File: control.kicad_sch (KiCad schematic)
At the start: 0 parts

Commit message: split into multiple sheets
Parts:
- added C1, C2: 10µF, Capacitor_SMD:C_0402_1005Metric, symbol Device:C_Small
- added C10, C8, C9: 4.7µF, Capacitor_SMD:C_0402_1005Metric, symbol Device:C_Small
- added C11: 10nF, Capacitor_SMD:C_0402_1005Metric, symbol Device:C_Small
- added C12: 1µF, Capacitor_SMD:C_0402_1005Metric, symbol Device:C_Small
- added C3, C4, C5, C6, C7: 100nF, Capacitor_SMD:C_0402_1005Metric, symbol Device:C_Small
- added F1: Fuse, symbol Device:Fuse
- added FB1: 100Ohm @ 100MHz, symbol Device:Ferrite_Bead_Small
- added J1: USB_OTG, symbol Connector:USB_OTG
- added J2: Conn_01x04_Male, symbol Connector:Conn_01x04_Male
- added J5: Conn_ARM_JTAG_SWD_10, symbol Connector:Conn_ARM_JTAG_SWD_10
- added JP1: SolderJumper_3_Bridged12, symbol Jumper:SolderJumper_3_Bridged12
- added JP2: SolderJumper_2_Open, symbol Jumper:SolderJumper_2_Open
- added R5: 10kΩ, symbol Device:R_Small
- added U2: AMS1117-3.3, Package_TO_SOT_SMD:SOT-223-3_TabPin2, symbol Regulator_Linear:AMS1117-3.3
- added U3: STM32F042C4Tx, Package_QFP:LQFP-48_7x7mm_P0.5mm, symbol MCU_ST_STM32F0:STM32F042C4Tx
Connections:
- new net: F1.2, FB1.1
- new net: C1.1, FB1.2, U2.3 (VI)
- new net: J2.1 (Pin_1), JP1.2 (C)
- new net +3V3: C10.1, C11.1, C12.1, C2.1, C3.1, C4.1, C5.1, C6.1, C7.1, C8.1, C9.1, J5.1 (VTref), JP1.1 (A), JP2.2 (B), U2.2 (VO), U3.1 (VBAT), U3.24 (VDD), U3.36 (VDDIO2), U3.48 (VDD), U3.9 (VDDA)
- new net +5V: F1.1, J1.1 (VBUS), JP1.3 (B)
- new net BOOT0: JP2.1 (A), R5.1, U3.44 (PF11)
- new net GND: C1.2, C10.2, C11.2, C12.2, C2.2, C3.2, C4.2, C5.2, C6.2, C7.2, C8.2, C9.2, J1.4 (ID), J1.5 (GND), J2.4 (Pin_4), J5.3 (GND), J5.5 (GND), J5.9 (GNDDetect), R5.2, U2.1 (GND), U3.23 (VSS), U3.35 (VSS), U3.47 (VSS), U3.8 (VSSA)
- new net NRST: J5.10 (~RESET~), U3.7 (NRST)
- new net SW1_ADC: U3.11 (PA1)
- new net SW1_DEN: U3.39 (PB3)
- new net SW1_IN: U3.20 (PB2)
- new net SWCLK: J5.4 (SWDCLK/TCK), U3.37 (PA14)
- new net SWDIO: J5.2 (SWDIO/TMS), U3.34 (PA13)
- new net UART_RX: J2.3 (Pin_3), U3.31 (PA10)
- new net UART_TX: J2.2 (Pin_2), U3.30 (PA9)
- new net USB_DM: J1.2 (D-), U3.32 (PA11)
- new net USB_DP: J1.3 (D+), U3.33 (PA12)
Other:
- note added: "Boot Option"
- note added: "Input Voltage Regulator"
- note added: "Power Supply Decoupling"
- note added: "SWD Debug"
- note added: "UART Communication"
- note added: "USB Connector"

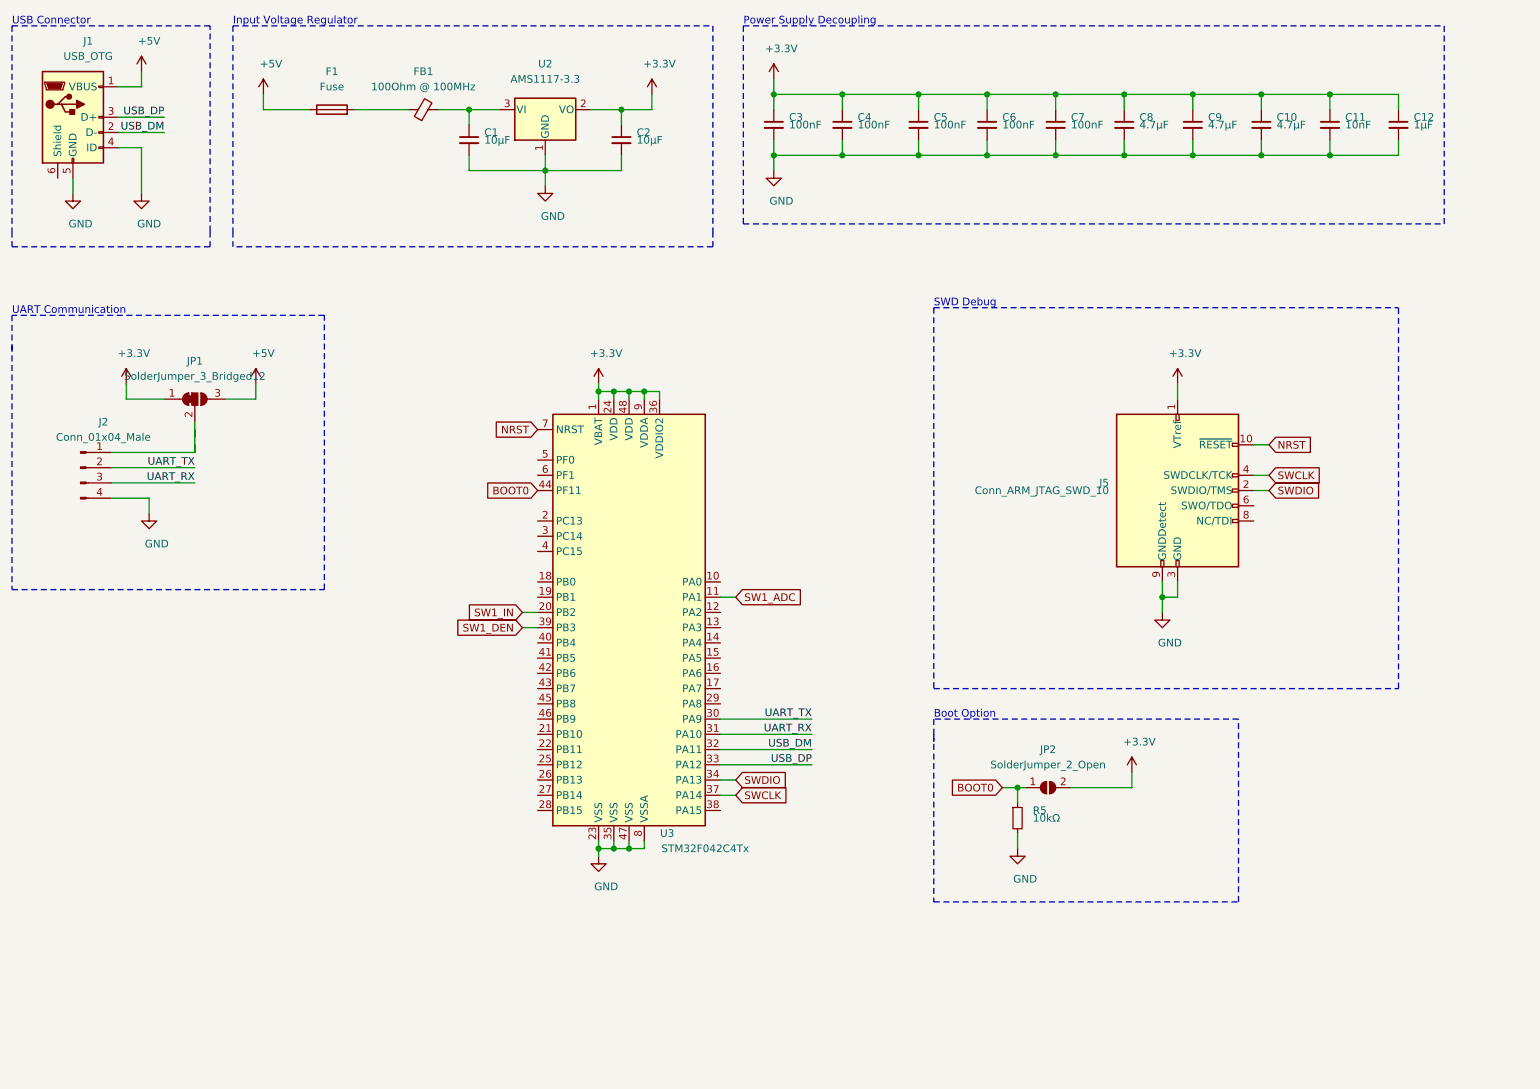
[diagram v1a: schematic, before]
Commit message: use USB-C and add analog filtering
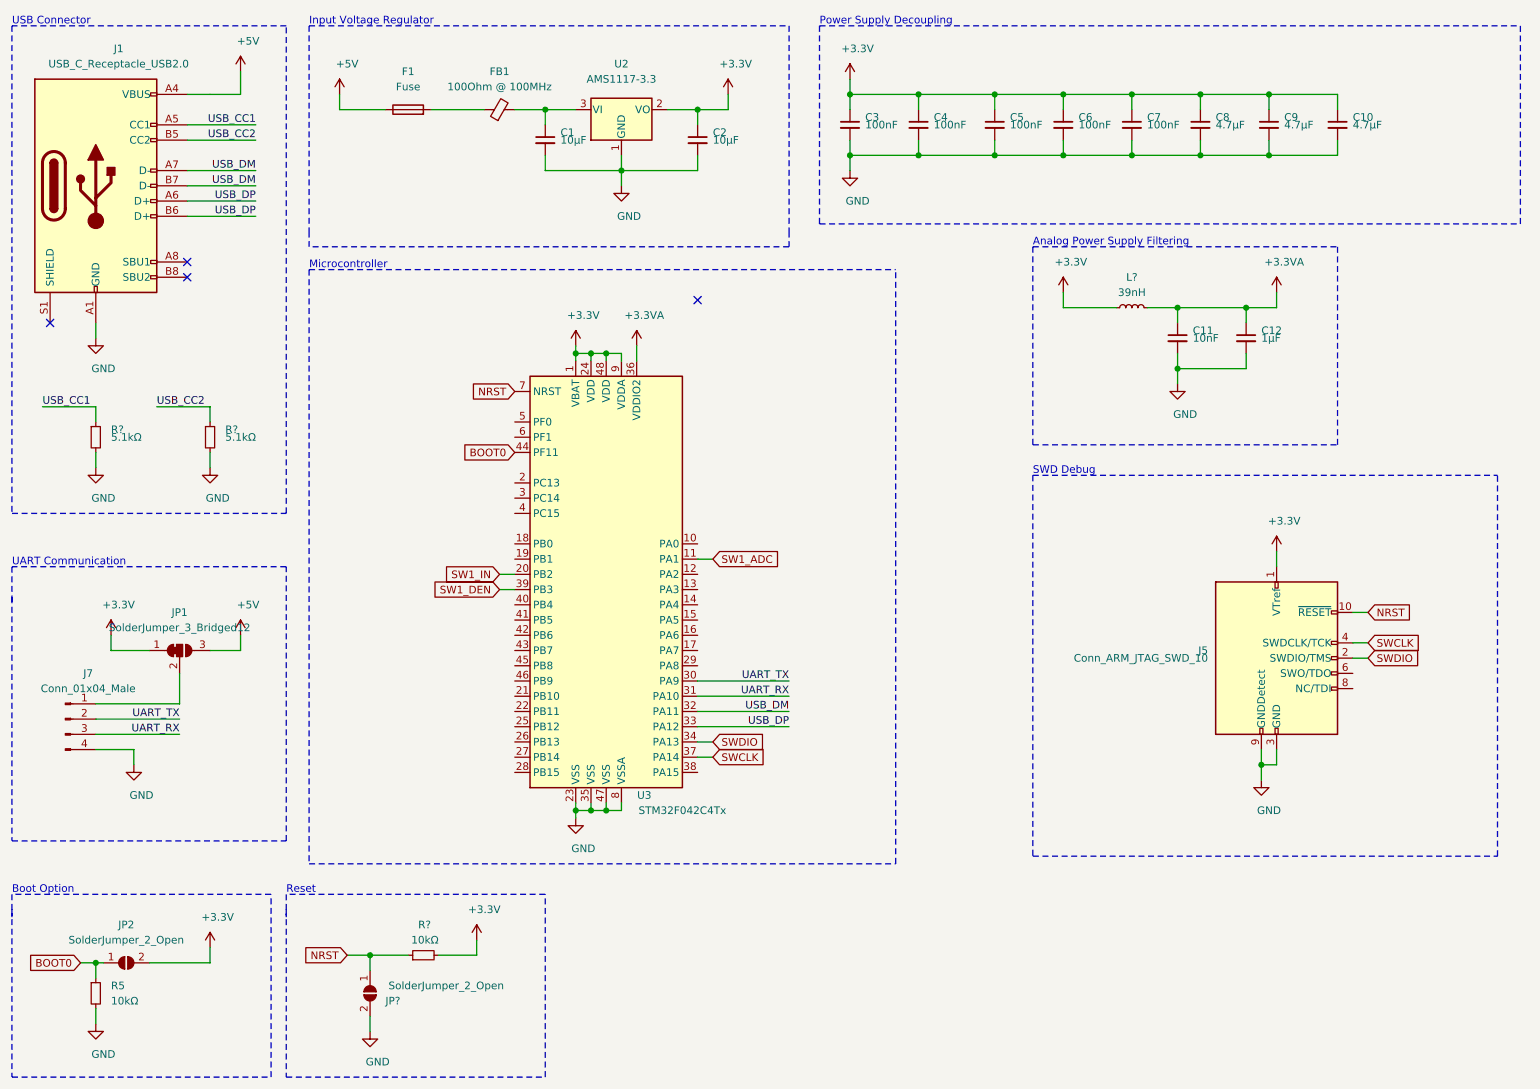
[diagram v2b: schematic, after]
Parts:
- removed J1: USB_OTG, symbol Connector:USB_OTG
- added J1: USB_C_Receptacle_USB2.0, symbol Connector:USB_C_Receptacle_USB2.0
- added JP?: SolderJumper_2_Open, Jumper:SolderJumper-2_P1.3mm_Open_RoundedPad1.0x1.5mm, symbol Jumper:SolderJumper_2_Open
- added L?: 39nH, symbol Device:L_Small
- added R? (x2): 5.1kΩ, symbol Device:R_Small
- added R?: 10kΩ, Resistor_SMD:R_0402_1005Metric, symbol Device:R_Small
- J5: footprint (none) -> Connector_PinHeader_1.27mm:PinHeader_2x05_P1.27mm_Vertical_SMD
- J7: renamed from J2; footprint (none) -> Connector_PinHeader_2.54mm:PinHeader_1x04_P2.54mm_Vertical
- JP1: footprint (none) -> Jumper:SolderJumper-3_P1.3mm_Bridged12_RoundedPad1.0x1.5mm_NumberLabels
- JP2: footprint (none) -> Jumper:SolderJumper-2_P1.3mm_Open_RoundedPad1.0x1.5mm
- R5: footprint (none) -> Resistor_SMD:R_0402_1005Metric
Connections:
- net +3V3: now also L?.1, R?.2; no longer C11.1, C12.1, U3.36 (VDDIO2)
- net +5V: now also J1.A4 (VBUS), J1.A9 (VBUS), J1.B4 (VBUS), J1.B9 (VBUS)
- net GND: now also J1.A1 (GND), J1.A12 (GND), J1.B1 (GND), J1.B12 (GND), JP?.2 (B), R?.2, R?.2
- net NRST: now also JP?.1 (A), R?.1
- net USB_DM: now also J1.A7 (D-), J1.B7 (D-)
- net USB_DP: now also J1.A6 (D+), J1.B6 (D+)
- new net +3.3VA: C11.1, C12.1, L?.2, U3.36 (VDDIO2)
- new net USB_CC1: J1.A5 (CC1), R?.1
- new net USB_CC2: J1.B5 (CC2), R?.1
- no-connect marks 0 -> 4
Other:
- note added: "Analog Power Supply Filtering"
- note added: "Microcontroller"
- note added: "Reset"
- moved on the sheet: C1, C10, C11, C12, C2, C3, C4, C5, C6, C7, C8, C9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

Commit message: complete current sense circuit, add leds
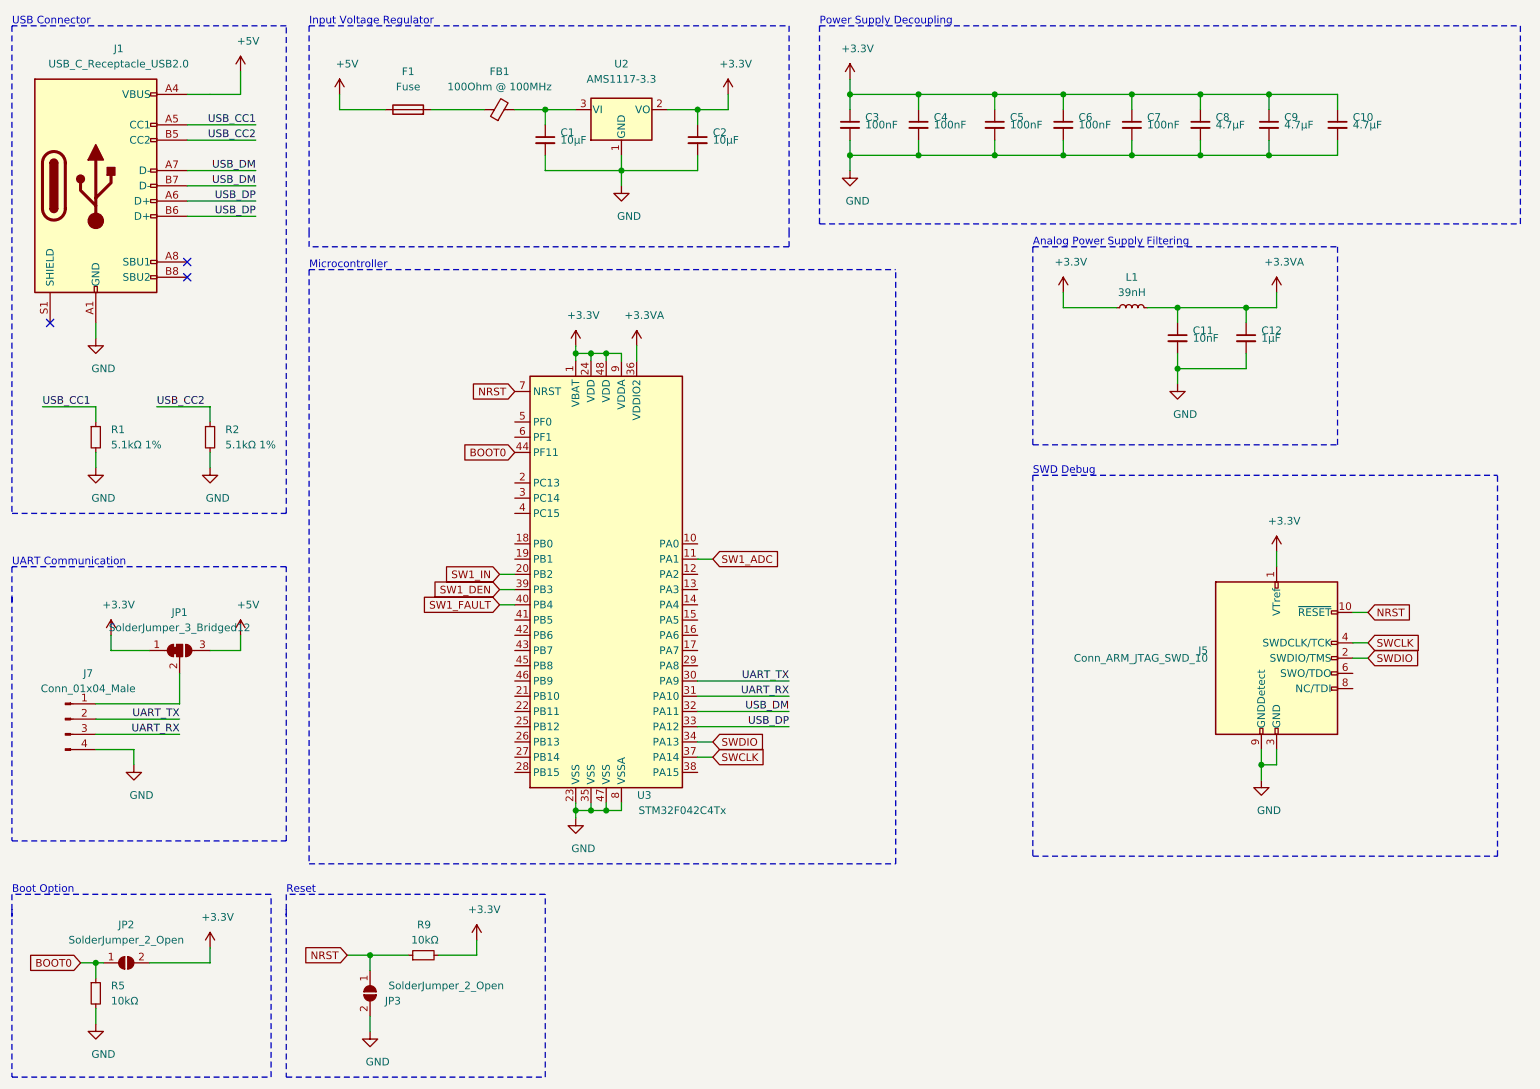
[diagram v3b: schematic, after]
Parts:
- R1, R2: renamed from R?; value 5.1kΩ -> 5.1kΩ 1%
- gave numbers to parts that had none: 3
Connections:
- net SW1_FAULT: now reaches U3.40 (PB4)
- no-connect marks 4 -> 3
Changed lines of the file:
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@@
   (no_connect (at 46.99 57.15))
   (no_connect (at 46.99 59.69))
-  (no_connect (at 132.08 63.5))
   (no_connect (at 24.13 67.31))
   (wire (pts (xy 22.86 81.28) (xy 31.75 81.28))
@@
     (stroke (width 0) (type solid) (color 0 0 0 0))
   )
+  (wire (pts (xy 99.06 114.3) (xy 101.6 114.3))
+    (stroke (width 0) (type solid) (color 0 0 0 0))
+  )
   (wire (pts (xy 101.6 31.75) (xy 106.68 31.75))
     (stroke (width 0) (type solid) (color 0 0 0 0))
@@
     (effects (font (size 1.27 1.27)) (justify right))
   )
+  (global_label "SW1_FAULT" (shape input) (at 99.06 114.3 180)
+    (effects (font (size 1.27 1.27)) (justify right))
+  )
   (global_label "NRST" (shape input) (at 101.6 78.74 180)
     (effects (font (size 1.27 1.27)) (justify right))
@@
   (symbol (lib_id "Device:L_Small") (at 204.47 64.77 90) (unit 1)
     (in_bom yes) (on_board yes)
-    (property "Reference" "L?" (id 0) (at 204.47 59.69 90))
+    (property "Reference" "L1" (id 0) (at 204.47 59.69 90))
     (property "Value" "39nH" (id 1) (at 204.47 62.23 90))
     (property "Footprint" "" (id 2) (at 204.47 64.77 0)
@@
   (symbol (lib_id "power:+3.3V") (at 95.25 170.18 0) (unit 1)
     (in_bom yes) (on_board yes)
-    (property "Reference" "#PWR?" (id 0) (at 95.25 173.99 0)
+    (property "Reference" "#PWR027" (id 0) (at 95.25 173.99 0)
       (effects (font (size 1.27 1.27)) hide)
     )
@@
   (symbol (lib_id "power:+3.3VA") (at 121.92 71.12 0) (unit 1)
     (in_bom yes) (on_board yes)
-    (property "Reference" "#PWR?" (id 0) (at 121.92 74.93 0)
+    (property "Reference" "#PWR028" (id 0) (at 121.92 74.93 0)
       (effects (font (size 1.27 1.27)) hide)
     )
@@
   (symbol (lib_id "power:+3.3V") (at 193.04 62.23 0) (unit 1)
     (in_bom yes) (on_board yes)
-    (property "Reference" "#PWR?" (id 0) (at 193.04 66.04 0)
+    (property "Reference" "#PWR029" (id 0) (at 193.04 66.04 0)
       (effects (font (size 1.27 1.27)) hide)
     )
@@
   (symbol (lib_id "power:+3.3VA") (at 228.6 62.23 0) (unit 1)
     (in_bom yes) (on_board yes)
-    (property "Reference" "#PWR?" (id 0) (at 228.6 66.04 0)
+    (property "Reference" "#PWR031" (id 0) (at 228.6 66.04 0)
       (effects (font (size 1.27 1.27)) hide)
     )
@@
   (symbol (lib_id "power:GND") (at 31.75 91.44 0) (unit 1)
     (in_bom yes) (on_board yes)
-    (property "Reference" "#PWR?" (id 0) (at 31.75 97.79 0)
+    (property "Reference" "#PWR01" (id 0) (at 31.75 97.79 0)
       (effects (font (size 1.27 1.27)) hide)
     )
@@
   (symbol (lib_id "power:GND") (at 50.8 91.44 0) (unit 1)
     (in_bom yes) (on_board yes)
-    (property "Reference" "#PWR?" (id 0) (at 50.8 97.79 0)
+    (property "Reference" "#PWR023" (id 0) (at 50.8 97.79 0)
       (effects (font (size 1.27 1.27)) hide)
     )
@@
   (symbol (lib_id "power:GND") (at 77.47 185.42 0) (unit 1)
     (in_bom yes) (on_board yes)
-    (property "Reference" "#PWR?" (id 0) (at 77.47 191.77 0)
+    (property "Reference" "#PWR025" (id 0) (at 77.47 191.77 0)
       (effects (font (size 1.27 1.27)) hide)
     )
@@
   (symbol (lib_id "power:GND") (at 212.09 77.47 0) (unit 1)
     (in_bom yes) (on_board yes)
-    (property "Reference" "#PWR?" (id 0) (at 212.09 83.82 0)
+    (property "Reference" "#PWR030" (id 0) (at 212.09 83.82 0)
       (effects (font (size 1.27 1.27)) hide)
     )
@@
   (symbol (lib_id "Device:R_Small") (at 31.75 86.36 0) (unit 1)
     (in_bom yes) (on_board yes)
-    (property "Reference" "R?" (id 0) (at 34.29 85.09 0)
-      (effects (font (size 1.27 1.27)) (justify left))
-    )
-    (property "Value" "5.1kΩ" (id 1) (at 34.29 86.36 0)
+    (property "Reference" "R1" (id 0) (at 34.29 85.09 0)
+      (effects (font (size 1.27 1.27)) (justify left))
+    )
+    (property "Value" "5.1kΩ 1%" (id 1) (at 34.29 87.63 0)
       (effects (font (size 1.27 1.27)) (justify left))
     )
@@
   (symbol (lib_id "Device:R_Small") (at 50.8 86.36 0) (unit 1)
     (in_bom yes) (on_board yes)
-    (property "Reference" "R?" (id 0) (at 53.34 85.09 0)
-      (effects (font (size 1.27 1.27)) (justify left))
-    )
-    (property "Value" "5.1kΩ" (id 1) (at 53.34 86.36 0)
+    (property "Reference" "R2" (id 0) (at 53.34 85.09 0)
+      (effects (font (size 1.27 1.27)) (justify left))
+    )
+    (property "Value" "5.1kΩ 1%" (id 1) (at 53.34 87.63 0)
       (effects (font (size 1.27 1.27)) (justify left))
     )
@@
   (symbol (lib_id "Device:R_Small") (at 86.36 172.72 90) (unit 1)
     (in_bom yes) (on_board yes)
-    (property "Reference" "R?" (id 0) (at 87.63 167.64 90)
+    (property "Reference" "R9" (id 0) (at 87.63 167.64 90)
       (effects (font (size 1.27 1.27)) (justify left))
     )
@@
   (symbol (lib_id "Jumper:SolderJumper_2_Open") (at 77.47 179.07 270) (unit 1)
     (in_bom yes) (on_board yes)
-    (property "Reference" "JP?" (id 0) (at 81.28 180.34 90))
+    (property "Reference" "JP3" (id 0) (at 81.28 180.34 90))
     (property "Value" "SolderJumper_2_Open" (id 1) (at 90.17 177.8 90))
     (property "Footprint" "Jumper:SolderJumper-2_P1.3mm_Open_RoundedPad1.0x1.5mm" (id 2) (at 77.47 179.07 0)
